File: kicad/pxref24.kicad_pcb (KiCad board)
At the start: 2 copper layers, 78.1 x 46.4 mm, 71 parts, among them P1 CONN_2X1, P2 CONN_1X1, P3 CONN_1X1, P5 CONN_1X1, P6 CONN_2X1, Q1 2N3904, U1 LTZ1000A, U2 LT1013, U30 LTC2057

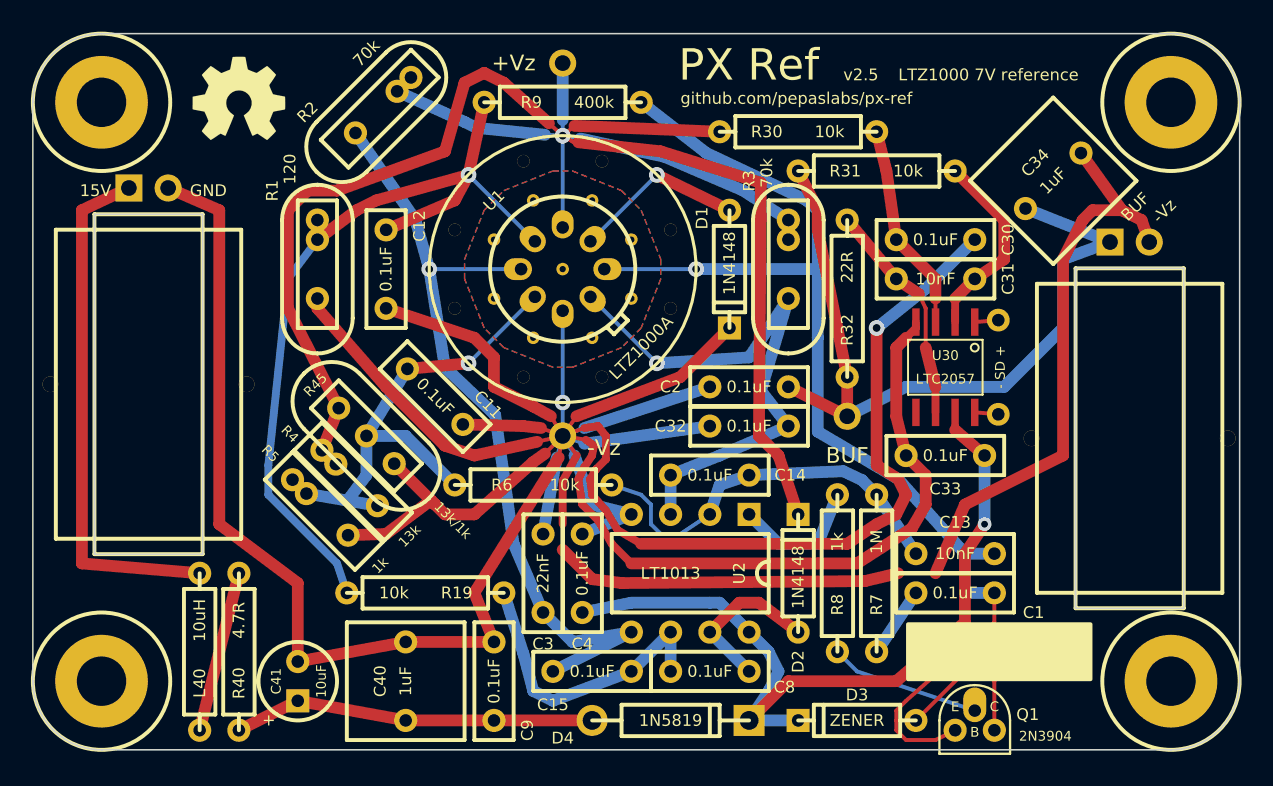
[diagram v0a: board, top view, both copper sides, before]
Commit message: splitting design into v2.4.x and v2.5.x
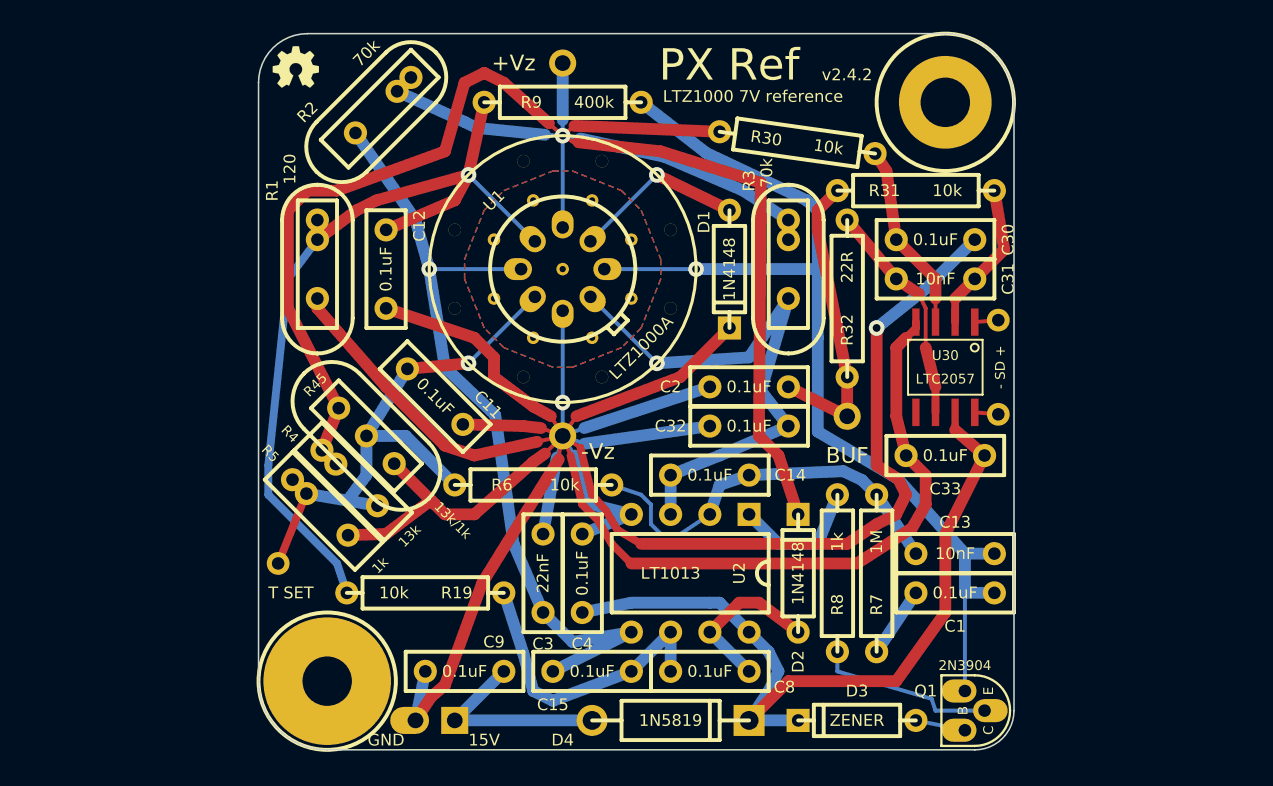
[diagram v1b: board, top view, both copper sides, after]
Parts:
- removed C34, C40: 1uF, BOXCAP_02_03_03_059A
- removed C41: 10uF, ELCAP_10_20_V_059A
- removed the G*** at (196.8, 71.5)
- removed the H*** at (188.0, 71.8)
- removed the H*** at (257.2, 109.2)
- removed L40: 10uH, R_AXIAL_0W25_059A_PL
- removed P6: CONN_2X1, ferrite_core_20x12_PL
- removed R40: 4.7R, R_AXIAL_0W25_059A_PL
- added G***: OSHW-logo_silkscreen-front_3mm, OSHW-logo_silkscreen-front_3mm, F.Cu at (200.5, 69.5)
- added H***: Val**, 1pin_032_058, F.Cu at (199.4, 101.6)
- added P4: CONN_1X1, 1pin_040_069, F.Cu at (208.3, 111.8)
- D1, D2, D3: footprint DIODE_SS_059A_03_PL -> DIODE_SS_059A_PL
- D4: footprint DIODE_1A_069A_04_PL -> DIODE_1A_069A_PL
- P1: value CONN_2X1 -> CONN_1X1; footprint ferrite_core_20x12_PL -> 1pin_040_069
- moved P1 29.4 mm to (210.8, 111.8), turned to 0 degrees
- moved H*** 14.6 mm to (242.6, 71.8)
- moved H1 14.6 mm to (202.6, 109.2)
- moved R31 2.84 mm to (245.7, 77.5)
- moved Q1 2.62 mm to (243.8, 109.9), turned to 90 degrees
- moved C9 2.01 mm to (211.5, 108.6), turned to 180 degrees
- turned R30 to 352 degrees
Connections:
- C9 pad 1: N-0000014 (its old number) -> N-000007
- D4 pad 1: N-0000014 (its old number) -> N-000007
- P1 pad 1: N-000008 (its old number) -> N-000007
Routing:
- net Vz- Sense: track 354.9 -> 240.3 mm
- net N-000008 (its old number): track 33.9 -> 0.00 mm
- net Vz+ Buf: track 50.2 -> 19.6 mm
- net N-0000014 (its old number): track 23.4 -> 0.00 mm
- net N-000007: track 0.00 -> 13.4 mm
- net N-000009: track 10.5 -> 0.00 mm
- net H+: track 76.9 -> 67.3 mm
- net N-0000018: track 9.83 -> 3.24 mm
- net (no net): track 3.06 -> 7.94 mm
- net N-000002: track 12.6 -> 9.88 mm
- net N-0000019: track 9.83 -> 11.6 mm
- net N-0000013: track 13.5 -> 12.2 mm
- net 15V: track 52.1 -> 51.3 mm, vias 1 -> 0
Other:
- board size 78.1 x 46.4 mm -> 48.9 x 46.4 mm
- board text added: "T SET"
- board text added: "v2.4.2"
- board text removed: "v2.5"

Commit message: v2.4.3
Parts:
- removed the H*** at (220.3, 75.6)
- removed the H*** at (210.8, 80.0)
- removed the H*** at (210.8, 85.1)
- removed the H*** at (224.8, 80.0)
- removed the H*** at (220.3, 89.5)
- removed the H*** at (215.3, 89.5)
- removed the H*** at (217.8, 82.5)
- added H***: Val**, Via_016, F.Cu at (220.7, 77.7)
- added H***: Val**, Via_016, F.Cu at (219.2, 77.2)
- added H***: Val**, Via_016, F.Cu at (216.4, 77.2)
- added H***: Val**, Via_016, F.Cu at (214.9, 77.7)
- added H***: Val**, Via_016, F.Cu at (222.5, 79.5)
- added H***: Val**, Via_016, F.Cu at (223.3, 81.3)
- added H***: Val**, Via_016, F.Cu at (213.1, 79.5)
- added H***: Val**, Via_016, F.Cu at (212.3, 81.0)
- added H***: Val**, Via_016, F.Cu at (223.3, 83.8)
- added H***: Val**, Via_016, F.Cu at (212.3, 83.8)
- added H***: Val**, Via_016, F.Cu at (213.1, 85.6)
- added H***: Val**, Via_016, F.Cu at (222.5, 85.6)
- added H***: Val**, Via_016, F.Cu at (220.7, 87.4)
- added H***: Val**, Via_016, F.Cu at (214.9, 87.4)
- added H***: Val**, Via_016, F.Cu at (219.2, 87.9)
- added H***: Val**, Via_016, F.Cu at (216.4, 87.9)
- added H***: Val**, Via_016, F.Cu at (216.9, 82.5)
- added H***: Val**, Via_016, F.Cu at (218.7, 82.5)
- added H***: Val**, Via_016, F.Cu at (217.8, 81.7)
- added H***: Val**, Via_016, F.Cu at (217.8, 83.4)
- moved H*** 5.85 mm to (210.8, 79.4)
- moved G*** 1.02 mm to (200.7, 70.5)
- moved H*** 0.64 mm to (242.6, 72.4)
- moved H*** 0.63 mm to (224.8, 85.7)
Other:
- board size 48.9 x 46.4 mm -> 48.9 x 45.7 mm
- board text added: "v2.4.3"
- board text removed: "v2.4.2"
